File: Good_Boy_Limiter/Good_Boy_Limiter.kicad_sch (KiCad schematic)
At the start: 34 parts, among them J2 Extra General Pins, Q2 AO3422, SW3 RESET1, SW4 BOOT1, U1 ESP32-S3-WROOM-1, U2 TC4427EOA_C636891, U3 LM2576HVR-12, U9 LM393DR2G

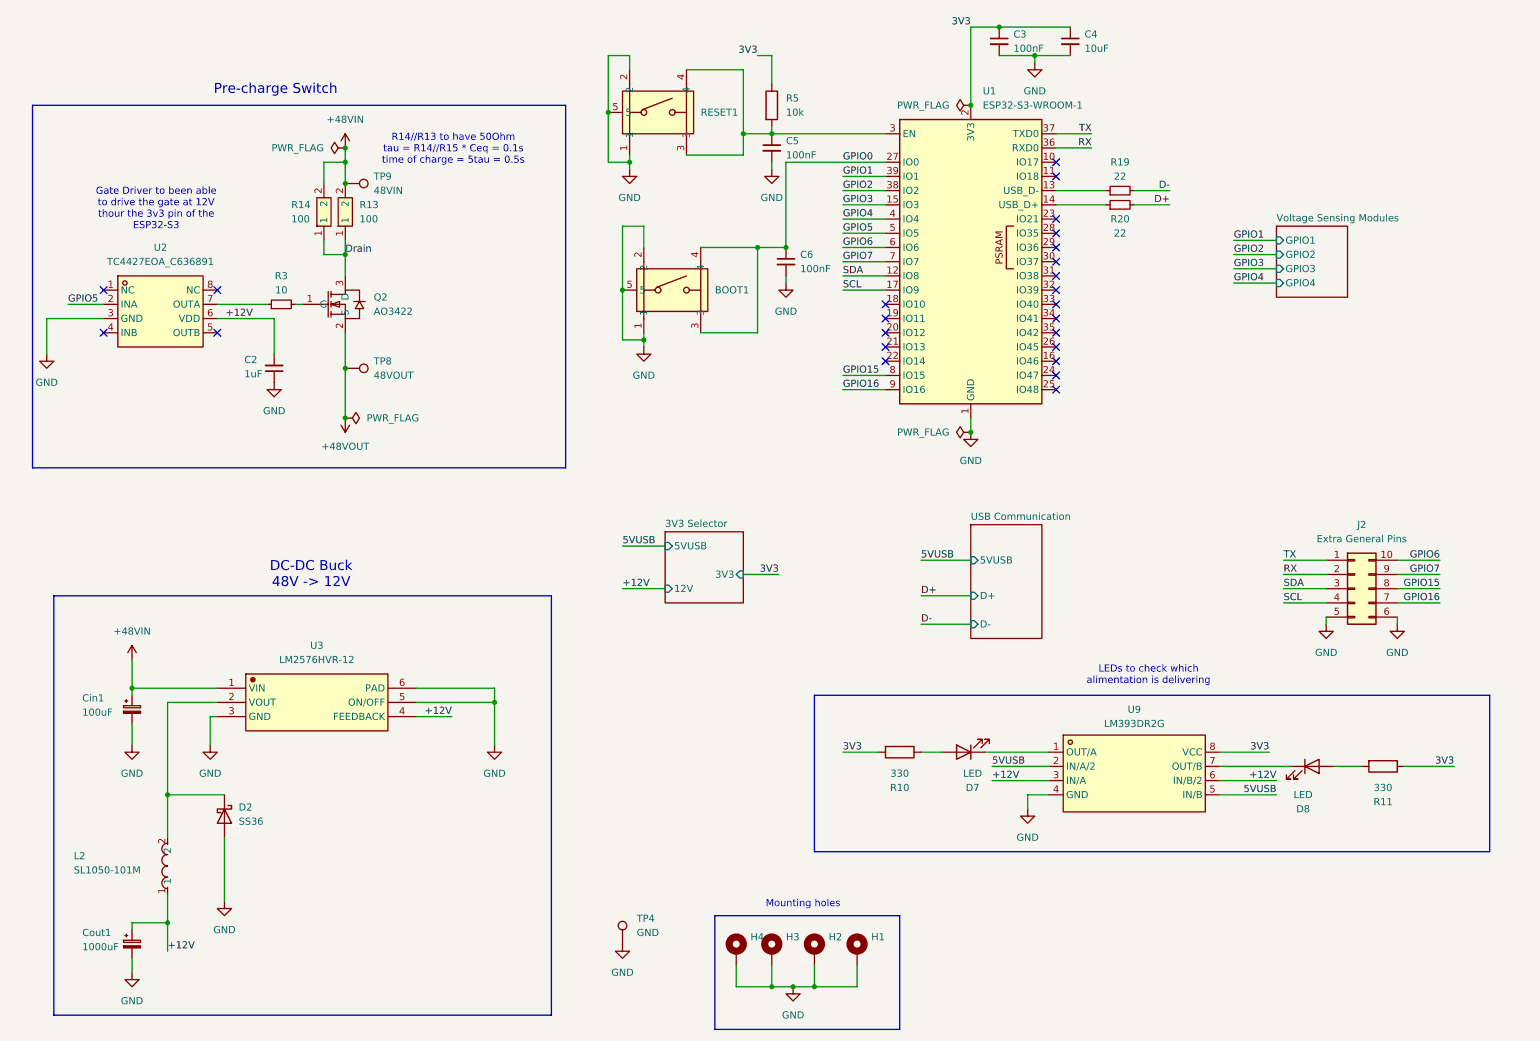
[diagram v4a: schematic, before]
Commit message: Added xt30 adn routed, ready for revision
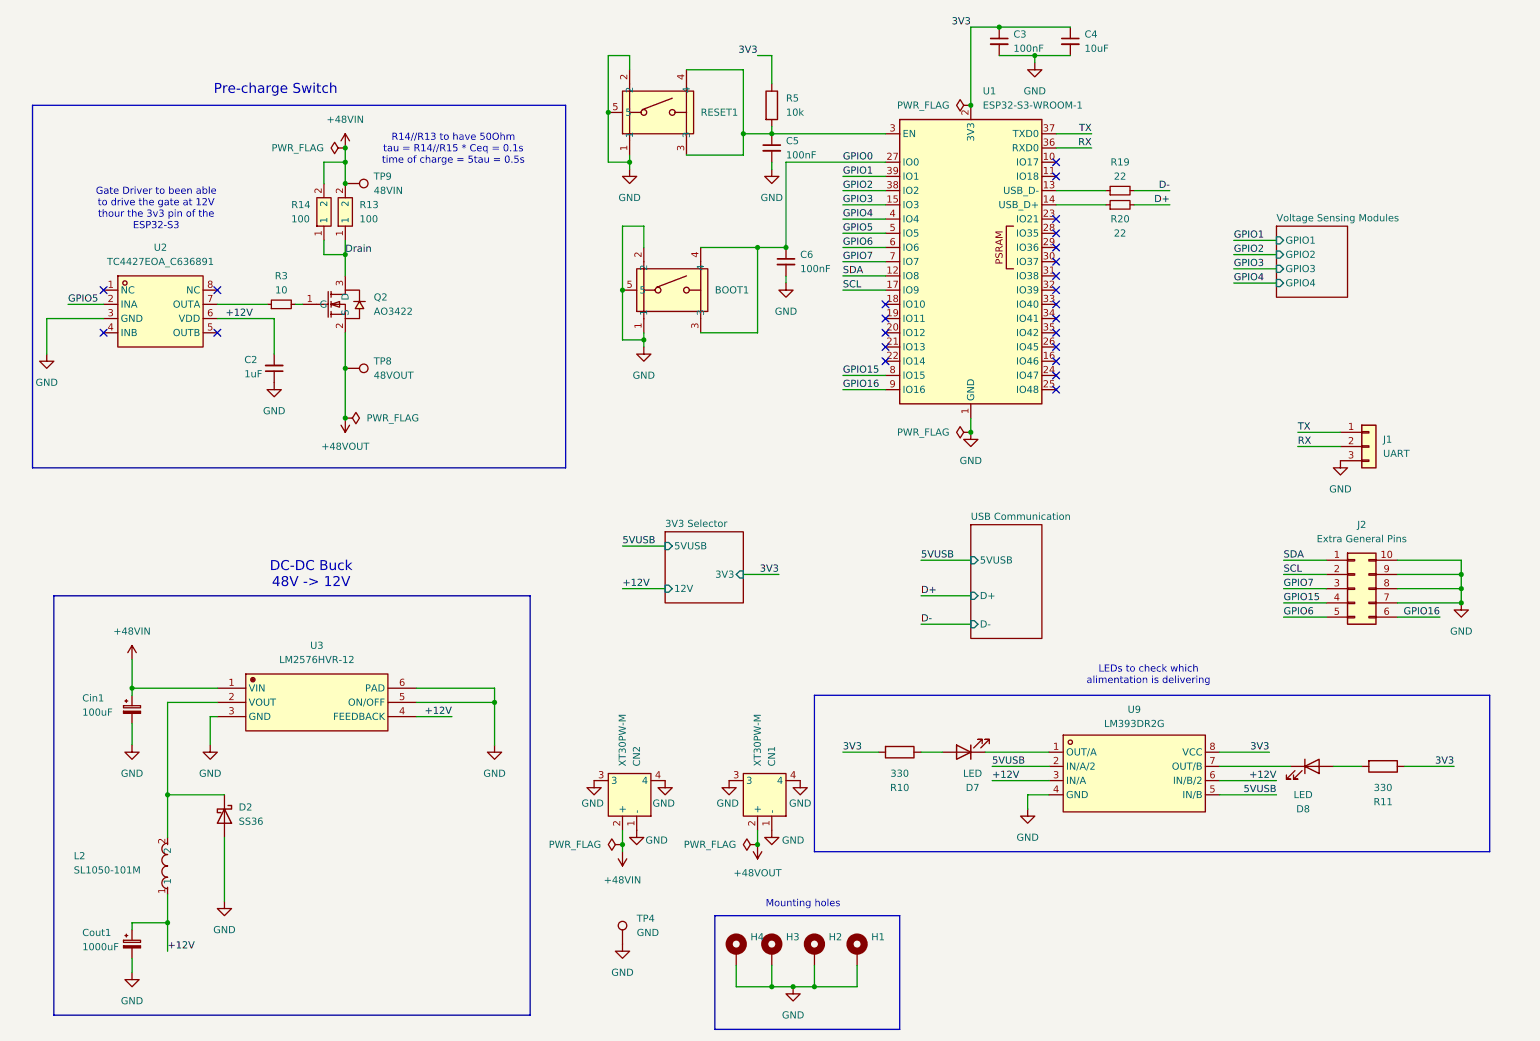
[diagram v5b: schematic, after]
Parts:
- added CN1, CN2: XT30PW-M, easyeda2kicad:CONN-TH_XT30PW-M, symbol easyeda2kicad:XT30PW-M
- added J1: UART, Connector_PinHeader_2.54mm:PinHeader_1x03_P2.54mm_Vertical, symbol Connector_Generic:Conn_01x03
- H1, H2, H3, H4: footprint MountingHole:MountingHole_3.2mm_M3_DIN965_Pad -> MountingHole:MountingHole_3.2mm_M3_Pad_Via
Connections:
- net +48VIN: now also CN2.2 (+)
- net +48VOUT: now also CN1.2 (+)
- net GND: now also J2.10 (Pin_10), J2.7 (Pin_7), J2.8 (Pin_8), J2.9 (Pin_9), CN1.1 (-), CN1.3, CN1.4, CN2.1 (-), CN2.3, CN2.4, J1.3 (Pin_3); no longer J2.5 (Pin_5), J2.6 (Pin_6)
- net GPIO15: now also J2.4 (Pin_4); no longer J2.8 (Pin_8)
- net GPIO16: now also J2.6 (Pin_6); no longer J2.7 (Pin_7)
- net GPIO6: now also J2.5 (Pin_5); no longer J2.10 (Pin_10)
- net GPIO7: now also J2.3 (Pin_3); no longer J2.9 (Pin_9)
- net RX: now also J1.2 (Pin_2); no longer J2.2 (Pin_2)
- net SCL: now also J2.2 (Pin_2); no longer J2.4 (Pin_4)
- net SDA: now also J2.1 (Pin_1); no longer J2.3 (Pin_3)
- net TX: now also J1.1 (Pin_1); no longer J2.1 (Pin_1)

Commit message: Finished e-scheme
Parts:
- removed C2: 1uF, Capacitor_SMD:C_0805_2012Metric_Pad1.18x1.45mm_HandSolder, symbol Device:C_Small
- removed Cin1: 100uF, easyeda2kicad:CAP-SMD_BD16.0-L17.0-W17.0-FD, symbol Device:C_Polarized_Small
- removed Cout1: 1000uF, easyeda2kicad:CAP-SMD_BD10.0-L10.3-W10.3-FD, symbol Device:C_Polarized_Small
- removed D2: SS36, Diode_SMD:D_SMA_Handsoldering, symbol Device:D_Schottky
- removed L2: SL1050-101M, easyeda2kicad:IND-SMD_L11.5-W10.5, symbol easyeda2kicad:SL1050-101M
- removed Q2: AO3422, easyeda2kicad:SOT-23_L2.9-W1.3-P1.90-LS2.4-BR, symbol easyeda2kicad:AO3422
- removed R13, R14: 100, easyeda2kicad:RES-SMD_L6.7-W4.0-LS7.9, symbol easyeda2kicad:SMW2100RJT
- removed R3: 10, LED_SMD:LED_0805_2012Metric_Pad1.15x1.40mm_HandSolder, symbol Device:R_Small
- removed U2: TC4427EOA_C636891, easyeda2kicad:SOIC-8_L4.9-W3.9-P1.27-LS6.0-TR, symbol easyeda2kicad:TC4427EOA_C636891
- removed U3: LM2576HVR-12, easyeda2kicad:TO-263-5_L10.2-W8.6-P1.70-LS14.4-TL, symbol easyeda2kicad:LM2576HVR-12
- added C13, C14: 2.2uF, Capacitor_SMD:C_1206_3216Metric, symbol Device:C_Small
- added C15: 47uF, easyeda2kicad:CAP-SMD_BD10.0-L10.3-W10.3-LS11.0-R-RD, symbol Device:C_Polarized_Small
- added Ca1: 3.3nF, Capacitor_SMD:C_0603_1608Metric, symbol Device:C_Small
- added Cb1: 56pF, Capacitor_SMD:C_0603_1608Metric, symbol Device:C_Small
- added Cbst1: 2.2nF, Capacitor_SMD:C_0603_1608Metric, symbol Device:C_Small
- added Cout1: 22uF, Capacitor_SMD:C_1210_3225Metric, symbol Device:C_Small
- added D11: SS510C, Diode_SMD:D_SMC, symbol Device:D_Schottky
- added Dsw1: SS510C, Diode_SMD:D_SMC_Handsoldering, symbol Device:D_Schottky
- added L3: 22uH, easyeda2kicad:IND-SMD_L11.5-W10.0, symbol Device:L_Small
- added Q4: AO3400A, easyeda2kicad:SOT-23-3_L2.9-W1.3-P1.90-LS2.4-BR, symbol easyeda2kicad:AO3400A
- added R13: 220, Resistor_SMD:R_0603_1608Metric, symbol Device:R
- added R14, R26: 10k, Resistor_SMD:R_0201_0603Metric_Pad0.64x0.40mm_HandSolder, symbol Device:R
- added R21: 100k, Resistor_SMD:R_0603_1608Metric_Pad0.98x0.95mm_HandSolder, symbol Device:R_Small
- added R22, R23: 453k, Capacitor_SMD:C_0603_1608Metric, symbol Device:R_Small
- added R24: 49.9k, Capacitor_SMD:C_0603_1608Metric, symbol Device:R_Small
- added R3: 50ohm, easyeda2kicad:RES-TH_BD9.0-L36.5-P40.50-D0.8, symbol easyeda2kicad:EWWR0010J50R0T9
- added U6: 1-178136-3, easyeda2kicad:1-178136-3_TYC, symbol easyeda2kicad:1-178136-3
- added U7: LM5013DDAR, easyeda2kicad:ESOP-8_L4.9-W3.9-P1.27-LS6.0-BL-EP-1, symbol easyeda2kicad:LM5013DDAR
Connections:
- net +12V: now also Ca1.1, Cout1.1, D11.1 (K), L3.2, R23.2, U6.3
- net +48VIN: now also C13.1, C14.1, C15.1, U7.2 (VIN), U7.3 (EN/UVLO)
- net +48VOUT: now also R3.1
- net 3V3: now also R14.1
- net GND: now also C13.2, C14.2, C15.2, Cout1.2, Dsw1.2 (A), Q4.2 (S), R21.2, R24.1, R26.2, U7.1 (GND), U7.9 (EP)
- net GPIO0: now also R14.2
- net GPIO6: now also R13.1; no longer J2.5 (Pin_5)
- new net: Q4.1 (G), R13.2, R26.1
- new net: D11.2 (A), Q4.3 (D), U6.2
- new net: Cb1.2, R23.1, R24.2, U7.5 (FB)
- new net: R21.1, U7.4 (RON)
- new net: Cbst1.2, U7.7 (BST)
- new net: Ca1.2, Cb1.1, R22.1
- new net In-rush controller/+48VOUT: R3.2
- new net LinOUT: Cbst1.1, Dsw1.1 (K), L3.1, R22.2, U7.8 (SW)
- no-connect marks 24 -> 22
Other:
- added sheet In-rush controller (inrush_controller.kicad_sch)
- note added: "Relay connector"
- note added: "XT30 IN/OUT connectors"
- note removed: "Gate Driver to been able to drive the gate at 12V thour the 3v3 pin of the ESP32-S3"
- note removed: "R14//R13 to have 50Ohm tau = R14//R15 * Ceq = 0.1s time of charge = 5tau = 0.5s"
- moved on the sheet: CN1, CN2, H1, H2, H3, H4, TP4, TP8, TP9

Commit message: started routing
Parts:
- J2: LCSC Part C5156677 -> (none)
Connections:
- net GPIO0: now also U1.10 (IO17); no longer U1.27 (IO0)
- net GPIO1: now also U1.11 (IO18); no longer U1.39 (IO1)
- net GPIO15: now also U1.24 (IO47); no longer U1.8 (IO15)
- net GPIO16: now also U1.25 (IO48); no longer U1.9 (IO16)
- net GPIO2: now also U1.13 (USB_D-); no longer U1.38 (IO2)
- net GPIO3: now also U1.14 (USB_D+); no longer U1.15 (IO3)
- net GPIO4: now also U1.23 (IO21); no longer U1.4 (IO4)
- net GPIO5: now also U1.28 (IO35); no longer U1.5 (IO5)
- net GPIO6: now also U1.29 (IO36); no longer U1.6 (IO6)
- net GPIO7: now also U1.30 (IO37); no longer U1.7 (IO7)
- net RX: no longer U1.36 (RXD0)
- net SCL: now also U1.32 (IO39); no longer U1.17 (IO9)
- net SDA: now also U1.31 (IO38); no longer U1.12 (IO8)
- net TX: now also U1.3 (EN); no longer U1.37 (TXD0)
- net at C5.1, R5.2, SW3.3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: now also U1.37 (TXD0); no longer U1.3 (EN)
- net at R19.1: now also U1.38 (IO2); no longer U1.13 (USB_D-)
- net at R20.1: now also U1.15 (IO3); no longer U1.14 (USB_D+)
- net GPIO14: now reaches U1.16 (IO46)
- net GPIO13: now reaches U1.26 (IO45)
- net GPIO10: now reaches U1.33 (IO40)
- net GPIO11: now reaches U1.34 (IO41)
- net GPIO12: now reaches U1.35 (IO42)
- no-connect marks 22 -> 17
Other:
- sheet Voltage Sensing Modules ports: added 3V3, GPIO10, GPIO11, GPIO12, GPIO13; removed GPIO1, GPIO2, GPIO3, GPIO4
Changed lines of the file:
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@@
 	)
 	(no_connect
-		(at 170.18 77.47)
-	)
-	(no_connect
 		(at 200.66 54.61)
 	)
 	(no_connect
-		(at 170.18 67.31)
-	)
-	(no_connect
 		(at 200.66 72.39)
 	)
@@
 	)
 	(no_connect
-		(at 170.18 72.39)
-	)
-	(no_connect
-		(at 170.18 74.93)
-	)
-	(no_connect
 		(at 200.66 82.55)
 	)
@@
 	)
 	(no_connect
-		(at 170.18 69.85)
-	)
-	(no_connect
 		(at 200.66 41.91)
 	)
 	(wire
 		(pts
+			(xy 162.56 72.39) (xy 170.18 72.39)
+		)
+		(stroke
+			(width 0)
+			(type default)
+		)
+	)
+	(wire
+		(pts
+			(xy 162.56 67.31) (xy 170.18 67.31)
+		)
+		(stroke
+			(width 0)
+			(type default)
+		)
+	)
+	(wire
+		(pts
 			(xy 121.92 180.34) (xy 121.92 184.15)
 		)
@@
 	(wire
 		(pts
+			(xy 162.56 74.93) (xy 170.18 74.93)
+		)
+		(stroke
+			(width 0)
+			(type default)
+		)
+	)
+	(wire
+		(pts
 			(xy 243.84 90.17) (xy 251.46 90.17)
 		)
@@
 	(wire
 		(pts
+			(xy 220.98 80.01) (xy 228.6 80.01)
+		)
+		(stroke
+			(width 0)
+			(type default)
+		)
+	)
+	(wire
+		(pts
 			(xy 200.66 36.83) (xy 207.01 36.83)
 		)
@@
 	(wire
 		(pts
+			(xy 162.56 77.47) (xy 170.18 77.47)
+		)
+		(stroke
+			(width 0)
+			(type default)
+		)
+	)
+	(wire
+		(pts
 			(xy 162.56 59.69) (xy 170.18 59.69)
 		)
@@
 	(wire
 		(pts
+			(xy 162.56 69.85) (xy 170.18 69.85)
+		)
+		(stroke
+			(width 0)
+			(type default)
+		)
+	)
+	(wire
+		(pts
 			(xy 269.24 54.61) (xy 269.24 49.53)
 		)
@@
 		)
 	)
-	(label "GPIO1"
-		(at 220.98 69.85 0)
+	(label "GPIO12"
+		(at 220.98 74.93 0)
 		(effects
 			(font
@@
 		)
 	)
-	(label "GPIO3"
-		(at 220.98 74.93 0)
+	(label "GPIO1"
+		(at 162.56 44.45 0)
 		(effects
 			(font
@@
 		)
 	)
-	(label "GPIO4"
-		(at 220.98 77.47 0)
+	(label "GPIO10"
+		(at 220.98 69.85 0)
 		(effects
 			(font
@@
 		)
 	)
-	(label "GPIO1"
-		(at 162.56 44.45 0)
+	(label "GPIO10"
+		(at 162.56 67.31 0)
 		(effects
 			(font
@@
 		)
 	)
-	(label "GPIO2"
-		(at 220.98 72.39 0)
+	(label "SCL"
+		(at 162.56 64.77 0)
 		(effects
 			(font
@@
 		)
 	)
-	(label "SCL"
-		(at 162.56 64.77 0)
+	(label "3V3"
+		(at 220.98 80.01 0)
 		(effects
 			(font
@@
 		)
 	)
+	(label "GPIO11"
+		(at 162.56 69.85 0)
+		(effects
+			(font
+				(size 1.27 1.27)
+			)
+			(justify left bottom)
+		)
+	)
 	(label "SDA"
 		(at 162.56 62.23 0)
@@
 		)
 	)
+	(label "GPIO13"
+		(at 220.98 77.47 0)
+		(effects
+			(font
+				(size 1.27 1.27)
+			)
+			(justify left bottom)
+		)
+	)
 	(label "GPIO16"
 		(at 269.24 123.19 180)
@@
 		)
 	)
+	(label "GPIO14"
+		(at 162.56 77.47 0)
+		(effects
+			(font
+				(size 1.27 1.27)
+			)
+			(justify left bottom)
+		)
+	)
 	(label "D-"
 		(at 200.66 120.65 0)
@@
 		)
 	)
+	(label "GPIO11"
+		(at 220.98 72.39 0)
+		(effects
+			(font
+				(size 1.27 1.27)
+			)
+			(justify left bottom)
+		)
+	)
 	(label "TX"
 		(at 207.01 36.83 180)
@@
 		)
 	)
+	(label "GPIO13"
+		(at 162.56 74.93 0)
+		(effects
+			(font
+				(size 1.27 1.27)
+			)
+			(justify left bottom)
+		)
+	)
 	(label "5VUSB"
 		(at 189.23 149.86 0)
@@
 		)
 	)
+	(label "GPIO12"
+		(at 162.56 72.39 0)
+		(effects
+			(font
+				(size 1.27 1.27)
+			)
+			(justify left bottom)
+		)
+	)
 	(label "GPIO16"
 		(at 162.56 82.55 0)
@@
 			)
 		)
-		(property "LCSC Part" "C5156677"
+		(property "LCSC Part" ""
 			(at 254 118.11 0)
 			(effects
@@
 		(lib_id "RF_Module:ESP32-S3-WROOM-1")
 		(at 185.42 59.69 0)
+		(mirror y)
 		(unit 1)
 		(exclude_from_sim no)
@@
 		(on_board yes)
 		(dnp no)
-		(fields_autoplaced yes)
 		(property "Reference" "U1"
-			(at 187.5633 29.21 0)
+			(at 183.2767 29.21 0)
 			(effects
 				(font
@@
 		)
 		(property "Value" "ESP32-S3-WROOM-1"
-			(at 187.5633 31.75 0)
+			(at 183.2767 31.75 0)
 			(effects
 				(font
@@
 	(sheet
 		(at 228.6 67.31)
-		(size 12.7 12.7)
+		(size 12.7 15.24)
 		(exclude_from_sim no)
 		(in_bom yes)
@@
 		)
 		(property "Sheetfile" "vsensing_modules.kicad_sch"
-			(at 228.6 80.5946 0)
+			(at 228.6 83.1346 0)
 			(effects
 				(font
@@
 			)
 		)
-		(pin "GPIO3" input
+		(pin "GPIO12" input
 			(at 228.6 74.93 180)
 			(effects
@@
 			)
 		)
-		(pin "GPIO4" input
+		(pin "GPIO13" input
 			(at 228.6 77.47 180)
 			(effects
@@
 			)
 		)
-		(pin "GPIO1" input
+		(pin "GPIO10" input
 			(at 228.6 69.85 180)
 			(effects
@@
 			)
 		)
-		(pin "GPIO2" input
+		(pin "GPIO11" input
 			(at 228.6 72.39 180)
 			(effects
 				(font
+					(size 1.27 1.27)
+				)
+				(justify left)
+			)
+		)
+		(pin "3V3" input
+			(at 228.6 80.01 180)
+			(effects
+				(font

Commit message: Routing Update
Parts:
- removed D7, D8: LED, LED_SMD:LED_0805_2012Metric_Pad1.15x1.40mm_HandSolder, symbol Device:LED
- removed R10, R11: 330, LED_SMD:LED_0805_2012Metric_Pad1.15x1.40mm_HandSolder, symbol Device:R
- removed U9: LM393DR2G, easyeda2kicad:SOIC-8_L5.0-W4.0-P1.27-LS6.0-BL, symbol easyeda2kicad:LM393DR2G
- added D16, D17, D9: LED, LED_SMD:LED_0805_2012Metric_Pad1.15x1.40mm_HandSolder, symbol Device:LED
- added R28: 4.8K, Resistor_SMD:R_0402_1005Metric, symbol Device:R_Small
- added R33: 1k, Resistor_SMD:R_0402_1005Metric, symbol Device:R_Small
- added R34: 330, Capacitor_SMD:C_0402_1005Metric, symbol Device:R
- C5: footprint Capacitor_SMD:C_0201_0603Metric_Pad0.64x0.40mm_HandSolder -> Capacitor_SMD:C_0402_1005Metric; LCSC Part C1590 -> C1525
- R14, R5: footprint Resistor_SMD:R_0201_0603Metric_Pad0.64x0.40mm_HandSolder -> Resistor_SMD:R_0603_1608Metric
- U6: LCSC Part (none) -> C591873
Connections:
- net +48VOUT: now also R28.2
- net 3V3: now also R34.1
- net GND: now also D16.1 (K), D17.1 (K), D9.1 (K), R33.1
- net GPIO0: now also U1.27 (IO0); no longer U1.10 (IO17)
- net GPIO1: now also U1.39 (IO1); no longer U1.11 (IO18)
- net GPIO10: now also U1.18 (IO10); no longer U1.33 (IO40)
- net GPIO11: now also U1.19 (IO11); no longer U1.34 (IO41)
- net GPIO12: now also U1.20 (IO12); no longer U1.35 (IO42)
- net GPIO13: now also U1.21 (IO13); no longer U1.26 (IO45)
- net GPIO14: now also U1.22 (IO14); no longer U1.16 (IO46)
- net GPIO15: now also U1.8 (IO15); no longer U1.24 (IO47)
- net GPIO16: now also U1.9 (IO16); no longer U1.25 (IO48)
- net GPIO2: now also U1.38 (IO2); no longer U1.13 (USB_D-)
- net GPIO3: now also U1.15 (IO3); no longer U1.14 (USB_D+)
- net GPIO4: now also U1.4 (IO4); no longer U1.23 (IO21)
- net GPIO5: now also U1.5 (IO5); no longer U1.28 (IO35)
- net GPIO6: now also U1.6 (IO6); no longer U1.29 (IO36)
- net GPIO7: now also U1.7 (IO7); no longer U1.30 (IO37)
- net RX: now also U1.36 (RXD0)
- net SCL: now also U1.17 (IO9); no longer U1.32 (IO39)
- net SDA: now also U1.12 (IO8); no longer U1.31 (IO38)
- net TX: now also U1.37 (TXD0); no longer U1.3 (EN)
- net at C5.1, R5.2, SW3.3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: now also U1.3 (EN); no longer U1.37 (TXD0)
- net at R20.1: now also U1.14 (USB_D+); no longer U1.15 (IO3)
- net at R19.1: now also U1.13 (USB_D-); no longer U1.38 (IO2)
- new net: D16.2 (A), R33.2
- new net: D17.2 (A), R34.2
- new net: D9.2 (A), R28.1
- new net GPIO17: U1.10 (IO17)
- new net GPIO18: U1.11 (IO18)
- new net GPIO38: U1.31 (IO38)
- new net GPIO39: U1.32 (IO39)
- new net GPIO40: U1.33 (IO40)
- new net GPIO41: U1.34 (IO41)
- new net GPIO42: U1.35 (IO42)
- new net GPIO47: U1.24 (IO47)
- new net GPIO48: U1.25 (IO48)
- no-connect marks 17 -> 8
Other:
- sheet Voltage Sensing Modules ports: added Vsens1, Vsens2, Vsens3, Vsens4; removed GPIO10, GPIO11, GPIO12, GPIO13
- note removed: "LEDs to check which alimentation is delivering"
